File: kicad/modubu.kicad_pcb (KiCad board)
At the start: 2 copper layers, 100 x 92 mm, 45 parts, among them J1 AudioJack4, J2 AudioJack4, SW1 SW_Push, SW10 SW_Push, SW11 SW_Push, SW12 SW_Push, SW13 SW_Push, SW14 SW_Push, SW15 SW_Push, SW16 SW_Push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

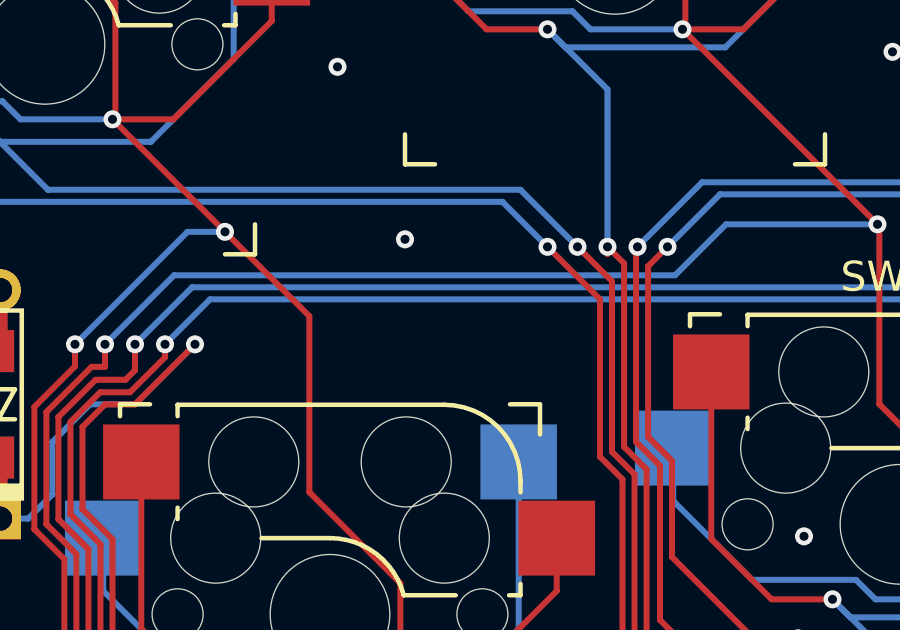
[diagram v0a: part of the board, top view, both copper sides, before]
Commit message: add position silkscreen
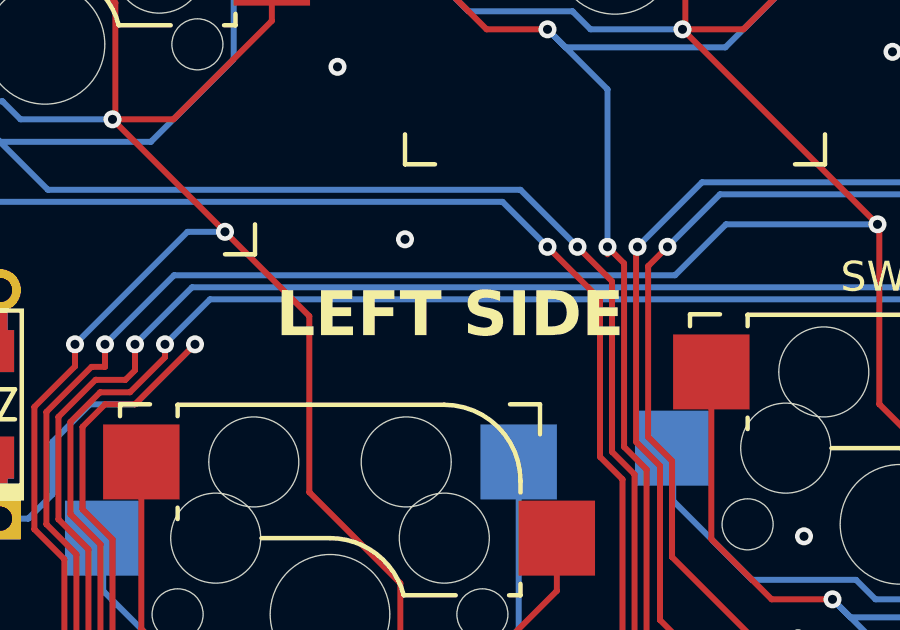
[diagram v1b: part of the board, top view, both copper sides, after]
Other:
- board text added: "LEFT SIDE"
- board text added: "RIGHT SIDE"
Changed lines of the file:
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@@
+		)
+	)
+	(gr_text "LEFT SIDE\n"
+		(at 85 93 0)
+		(layer "F.SilkS")
+		(effects
+			(font
+				(size 1.5 1.5)
+				(thickness 0.3)
+				(bold yes)
+			)
 		)
 	)
@@
 			)
 			(justify mirror)
+		)
+	)
+	(gr_text "RIGHT SIDE\n"
+		(at 85 93 -0)
+		(layer "B.SilkS")
+		(effects
+			(font
+				(size 1.5 1.5)
+				(thickness 0.3)
+				(bold yes)
+			)
+			(justify mirror)

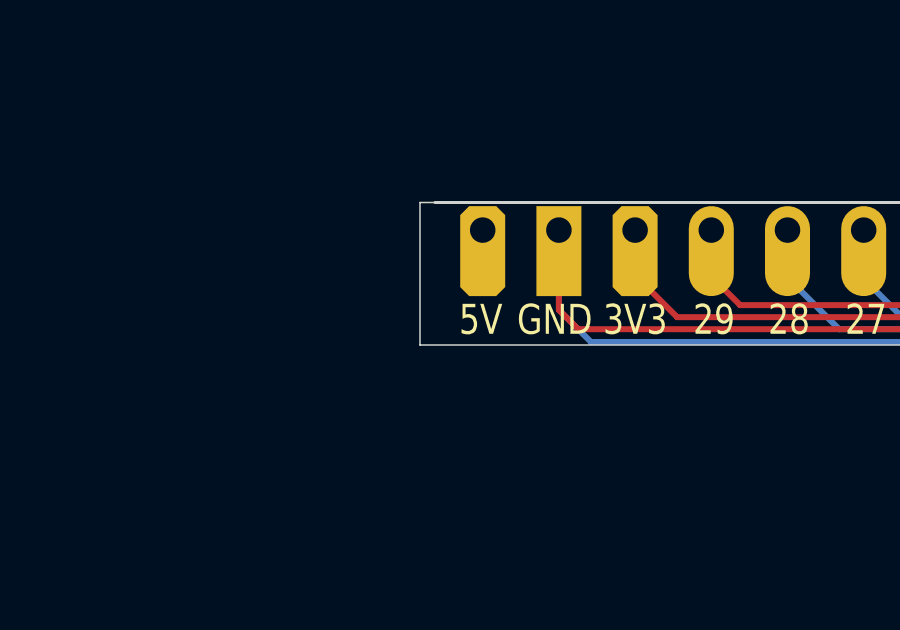
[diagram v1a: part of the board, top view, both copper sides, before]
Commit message: edit gerber ground via
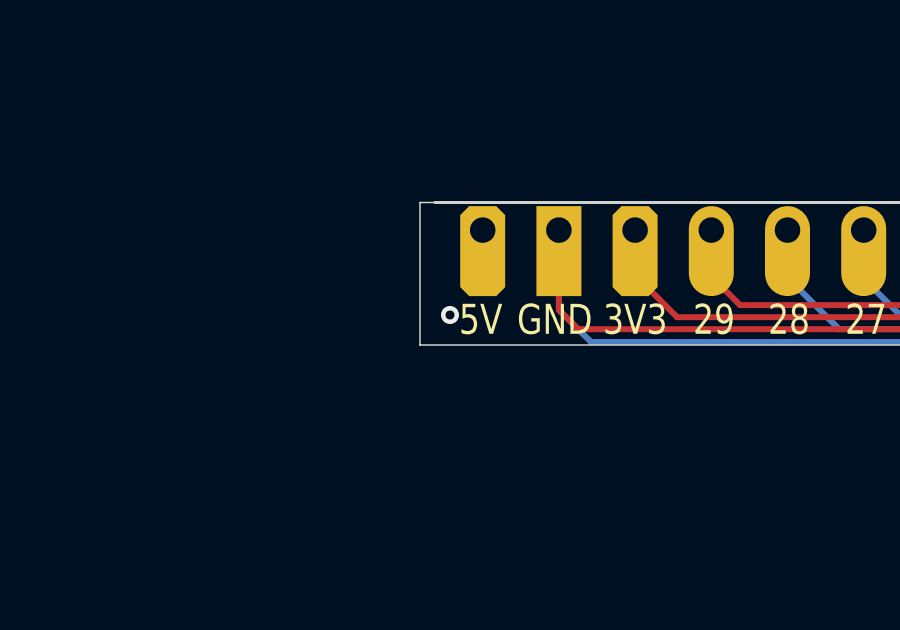
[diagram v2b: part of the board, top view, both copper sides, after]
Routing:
- net GND: vias 40 -> 41
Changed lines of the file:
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@@
+	)
+	(via
+		(at 56.5 137.5)
+		(size 0.6)
+		(drill 0.3)
+		(layers "F.Cu" "B.Cu")
+		(net 12)
 	)
 	(via
